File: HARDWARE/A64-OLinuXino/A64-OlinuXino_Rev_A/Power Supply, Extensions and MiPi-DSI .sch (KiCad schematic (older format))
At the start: 140 parts, among them Q2 MC-306_32.768KHZ/SMD_8038/6pF, Q3 4SB24.000F20E15/5x3.2mm/20ppm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, T1 WPM1481, U1 AllWinner-A64(FBGA396), U13 MT3608(SOT23-6), U14 AXP803

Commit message: A64-OLinuXino component placement, all components libraries updated
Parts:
- removed L15: FB0805/600R/2A, symbol L
- D1: renamed from D3; footprint (none) -> OLIMEX_Diodes-FP:DO214AA
- D4: footprint (none) -> OLIMEX_Diodes-FP:SOD-123_1C-2A_KA
- DBG_UART1: footprint (none) -> OLIMEX_Connectors-FP:HN1x3
- FET2: footprint (none) -> OLIMEX_Transistors-FP:SOT23
- FUSE2: footprint (none) -> OLIMEX_Devices-FP:FUSE-5025
- GPIO1: value GBH-254-SMT-40 -> NA(HN2x20); footprint (none) -> OLIMEX_Connectors-FP:HN2x20
- L14: renamed from L17; footprint (none) -> OLIMEX_RLC-FP:CD32
- L15: renamed from L18; footprint (none) -> OLIMEX_RLC-FP:CD42(43)
- L16: renamed from L14; footprint (none) -> OLIMEX_RLC-FP:YS75_7X8MM
- L17: renamed from L19; footprint (none) -> OLIMEX_RLC-FP:CD42(43)
- L18: renamed from L16; footprint (none) -> OLIMEX_RLC-FP:CD42(43)
- L19: renamed from L20; footprint (none) -> OLIMEX_RLC-FP:CD32
- L20: renamed from L21; footprint (none) -> OLIMEX_RLC-FP:CD32
- LIPO_BAT1: footprint (none) -> OLIMEX_Connectors-FP:LIPO_BAT-CON2DW02R
- MIPI-DSI1: value GPH127SMT-02X10(PA-V16X-2X10-LF) -> PV-WZA21-20-LF; footprint (none) -> OLIMEX_Connectors-FP:FPV-WZA21-20-LF
- PWR1: footprint (none) -> OLIMEX_Connectors-FP:PWR_JACK_UNI_MILLING
- PWRLED1: footprint (none) -> OLIMEX_LEDs-FP:LED_0603_KA
- PWRON1, RESET1, UBOOT1: footprint (none) -> OLIMEX_Buttons-FP:WS_TAKT_6X3,5_SMD_NOCREAM
- Q2: footprint (none) -> OLIMEX_Crystal-FP:MC306-HS
- Q3: footprint (none) -> OLIMEX_Crystal-FP:Q5x3.25
- RM14: footprint (none) -> OLIMEX_RLC-FP:RA0805_(4X0402)_xx
- T1: value WPM1481 -> WPM1481(DFN2X2-6L); footprint (none) -> OLIMEX_Transistors-FP:DFN2x2-6L
- U1: footprint (none) -> OLIMEX_IC-FP:FBGA396
- U13: footprint (none) -> OLIMEX_IC-FP:SOT23-6
- U14: value AXP803 -> AXP803(QFN68_8x8mm); footprint (none) -> OLIMEX_IC-FP:QFN68
- UEXT1: footprint (none) -> OLIMEX_Connectors-FP:GBH-254-SMT-10
- VCC-PE:2.8V/3.3V1: footprint (none) -> OLIMEX_Jumpers-FP:SJ_2_SMALL_12_TIED
- renumbered C171 to C115, C172 to C116, C173 to C117, C117 to C118, C118 to C119, C174 to C120, C133 to C121, C137 to C122, C175 to C123, C134 to C124, C138 to C125, C139 to C126, C176 to C127, C135 to C128, C140 to C129, C177 to C130, C141 to C131, C178 to C132, C142 to C133, C179 to C134, C136 to C135, C143 to C136, C180 to C137, C123 to C138, C144 to C139, C119 to C140, C120 to C141, C181 to C142, C115 to C143, C124 to C144, C182 to C146, C125 to C147, C183 to C148, C130 to C149, C146 to C150, C131 to C151, C132 to C152, C147 to C153, C148 to C154, C184 to C155, C121 to C156, C149 to C157, C185 to C158, C150 to C159, C186 to C160, C151 to C161, C152 to C162, C187 to C163, C153 to C164, C154 to C165, C188 to C166, C155 to C167, C189 to C168, C126 to C169, C156 to C170, C127 to C171, C157 to C172, C128 to C173, C158 to C174, C129 to C175, C159 to C176, C122 to C177, C160 to C178, C161 to C179, C116 to C180, C162 to C181, C163 to C182, C166 to C183, C167 to C184, C168 to C185, C190 to C186, C169 to C187, C191 to C188, C192 to C189, C193 to C190, C194 to C191, C195 to C192, C170 to C193, C164 to C194, C165 to C195, D1 to D2, D2 to D3, R76 to R74, R90 to R75, R91 to R76, R92 to R77, R87 to R78, R93 to R79, R74 to R80, R75 to R81, R80 to R82, R81 to R83, R88 to R84, R82 to R85, R83 to R86, R84 to R87, R85 to R88, R77 to R89, R86 to R90, R78 to R91, R89 to R92, R94 to R93, R95 to R94, R79 to R95
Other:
- note added: "GFC STILL NOT READ!"
- note added: "Notes:\n1.PC4 and PC7 could be used only when \nNAND Flash is not populated!\n2.VCC-PL is 1.8V, VCC-PE is 2.8V(default),\nVCC-PB and VCC-PC are 3.3V."
- note added: "The schematic was checked\nfrom Root up to Here!!!!!"
- note removed: "Note:\nPC4 and PC7 could be used only when \nNAND Flash is not populated!"

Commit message: A64-OLinuXino update
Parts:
- added C197: 100nF, OLIMEX_RLC-FP:C_0402_5MIL_DWS, symbol C
- added HSIC1: B4B-PH-K-S, OLIMEX_Connectors-FP:B4B-PH-K-S, symbol CON4
- added HSIC_E1: Opened, OLIMEX_Jumpers-FP:SJ, symbol SJ
- added R101, R102: NA(2.2k), OLIMEX_RLC-FP:R_0402_5MIL_DWS, symbol R
- added R103: NA(100k), OLIMEX_RLC-FP:R_0402_5MIL_DWS, symbol R
- added R104: NA(10k), OLIMEX_RLC-FP:R_0402_5MIL_DWS, symbol R
- PWRON1, RESET1, UBOOT1: footprint OLIMEX_Buttons-FP:WS_TAKT_6X3,5_SMD_NOCREAM -> OLIMEX_Buttons-FP:uTACTIL
- R74, R82: value 1k -> 2.2k; footprint OLIMEX_RLC-FP:R_0603_5MIL_DWS -> OLIMEX_RLC-FP:R_0402_5MIL_DWS
- R75, R76, R77, R79, R80, R81, R83, R84, R85, R86, R87, R88, R89, R90, R91, R92, R95: footprint OLIMEX_RLC-FP:R_0603_5MIL_DWS -> OLIMEX_RLC-FP:R_0402_5MIL_DWS
- R78: footprint OLIMEX_RLC-FP:R_0603_5MIL_DWS -> OLIMEX_RLC-FP:R_1206_5MIL_DWS
- UEXT1: footprint OLIMEX_Connectors-FP:GBH-254-SMT-10 -> OLIMEX_Connectors-FP:HN2x5
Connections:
- net +1.5V: now also U14.8 (DCDC5)
- net +3.0VA: now also R103.1
- net 1.1V_SYS: now also U14.9 (DCDC6)
- net 1.2V_HSIC: now also C197.1, HSIC_E1.1
- net 3.0V_RTC: now also R104.1
- net AP-RESET#: now also R104.2
- net GND: now also C197.2, HSIC1.4
- net KEYADC: now also R103.2
- net PE14: now also R101.1
- net PE15: now also R102.1
- net at L20.1, U14.10 (LX6): no longer U14.9 (DCDC6)
- net at L19.1, U14.7 (LX5): no longer U14.8 (DCDC5)
- net at C194.2, U1.U18 (VCC-PE), VCC-PE:2.8V/3.3V1.2: now also R101.2, R102.2
- net at U1.G19 (HSIC-DAT): now also HSIC1.3
- net at U1.H19 (HSIC-STR): now also HSIC1.2
- new net: HSIC1.1, HSIC_E1.2
- no-connect marks 4 -> 2
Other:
- note added: "+5VDC ONLY!!!"
- note added: "DC5SET DDR3-VCC\nFloating 1.24V\nGND 1.50V\nVINT 1.36V"
- note added: "DDR3-VCC"
- note added: "Notes:\n1.PC4 and PC7 could be used only when \nNAND Flash is not populated!\n2. VCC-PE is 2.8V(default),\nVCC-PB, VCC-PC and VCC-PL are 3.3V."
- note added: "VCC-PL=3.3V"
- note removed: "Notes:\n1.PC4 and PC7 could be used only when \nNAND Flash is not populated!\n2.VCC-PL is 1.8V, VCC-PE is 2.8V(default),\nVCC-PB and VCC-PC are 3.3V."
- note removed: "VCC-PL=1.8V"

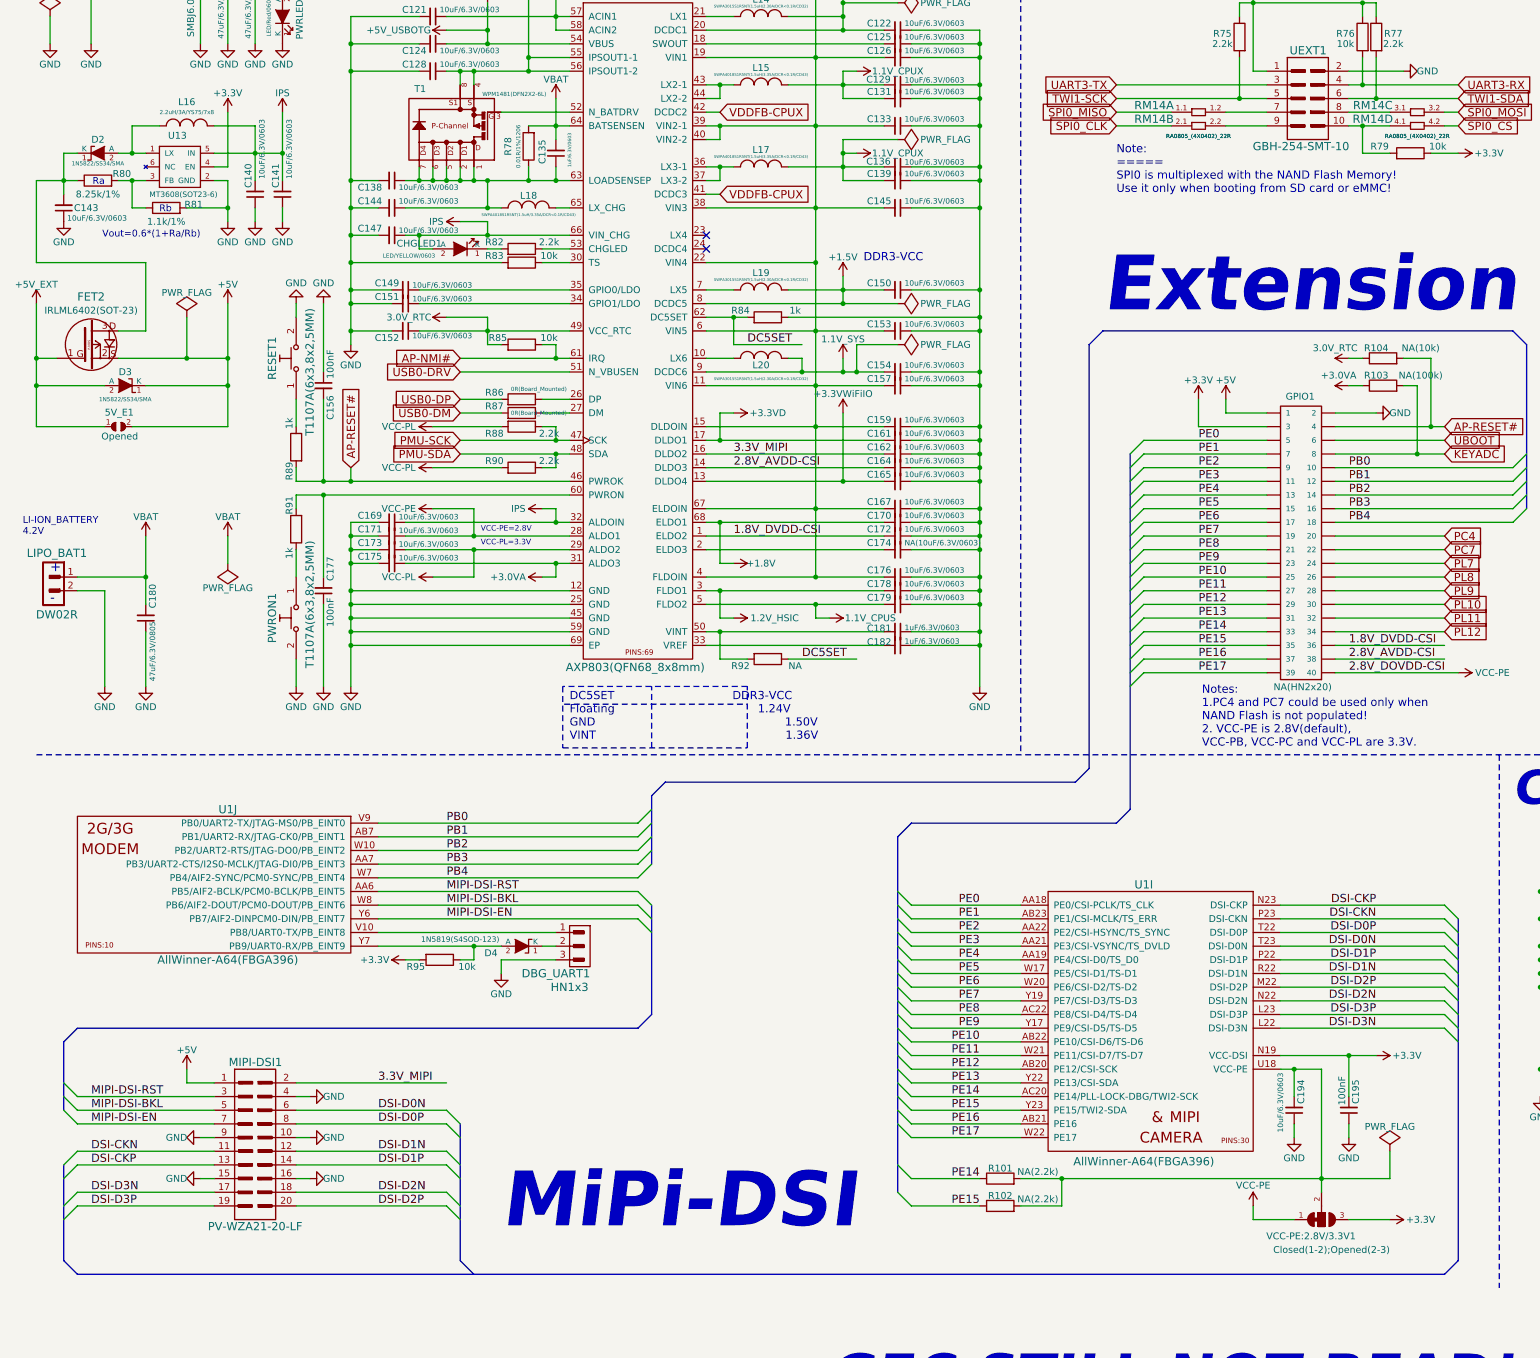
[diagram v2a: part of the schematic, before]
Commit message: A64-OLinuXino routing completed
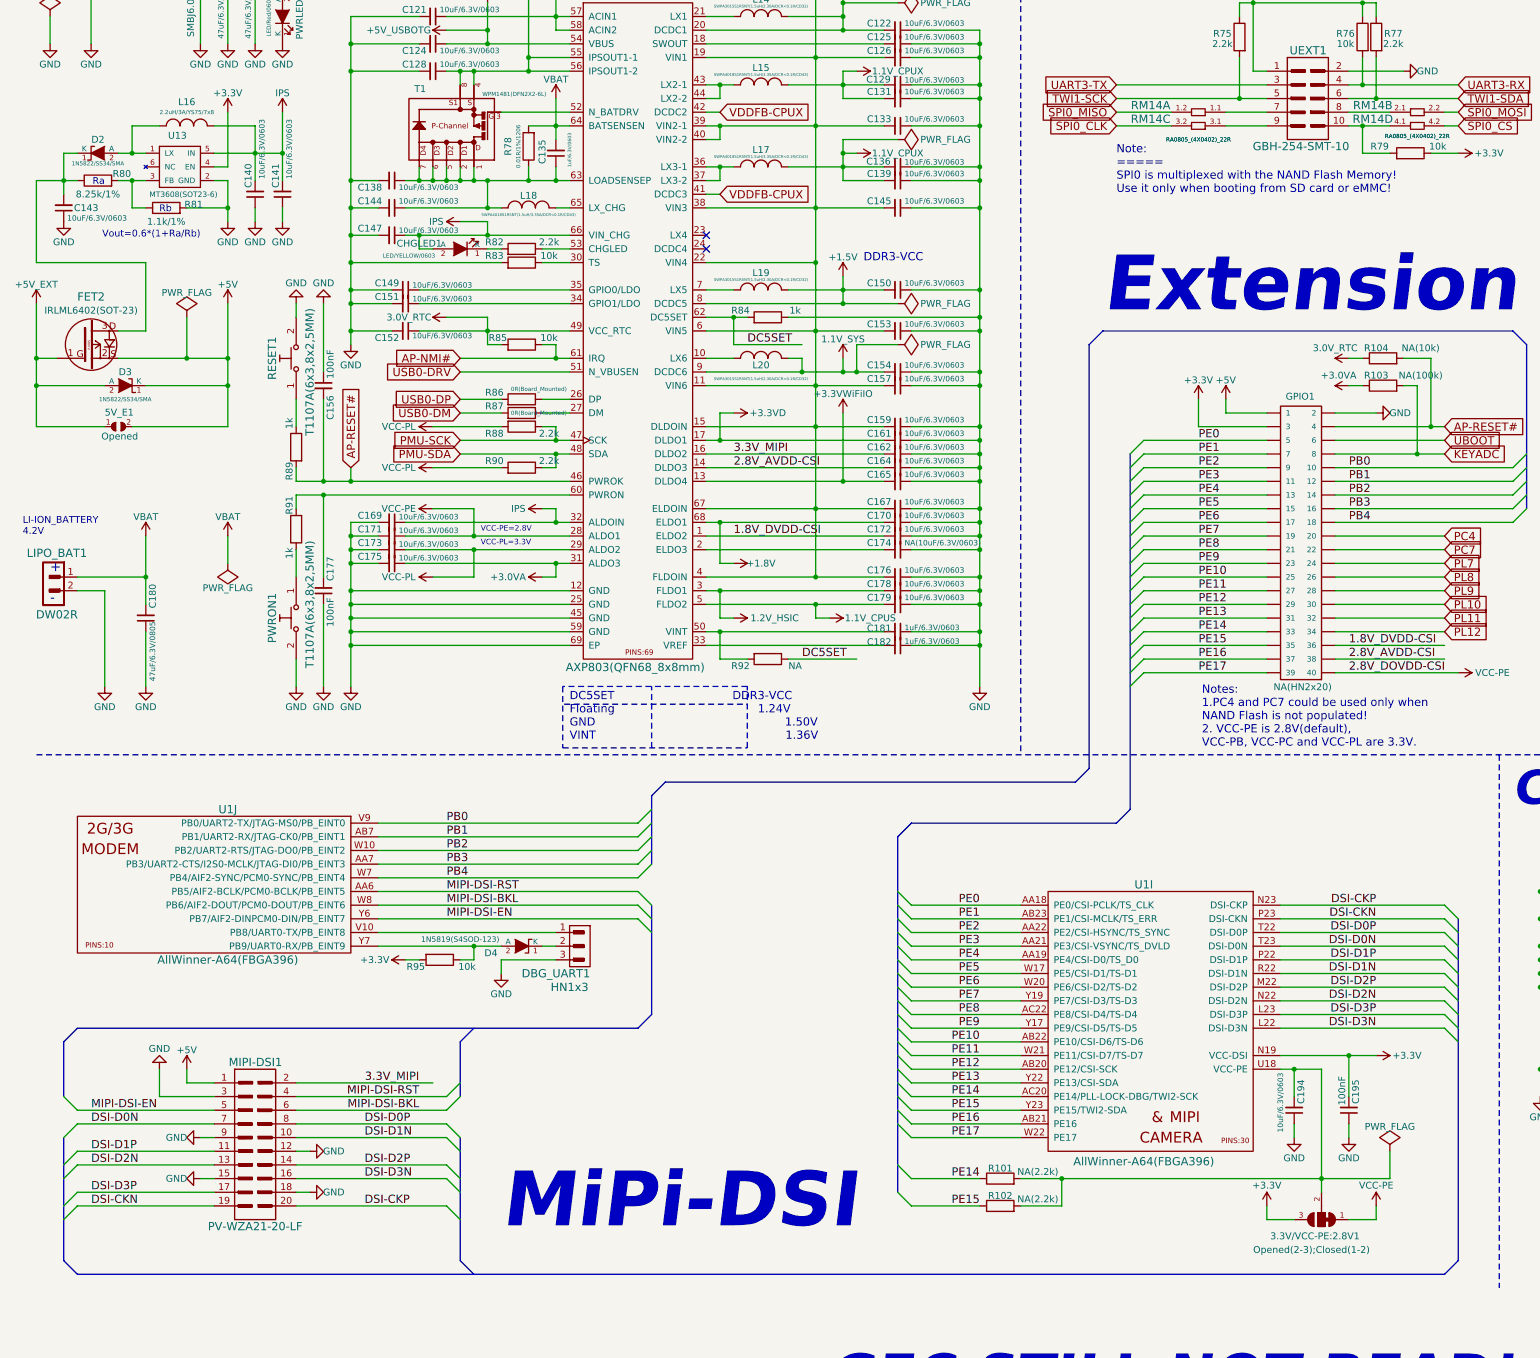
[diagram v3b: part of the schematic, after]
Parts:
- 3.3V/VCC-PE:2.8V1: renamed from VCC-PE:2.8V/3.3V1; value Closed(1-2);Opened(2-3) -> Opened(2-3);Closed(1-2)
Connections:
- net DSI-CKN: now also MIPI-DSI1.19; no longer MIPI-DSI1.11
- net DSI-CKP: now also MIPI-DSI1.20; no longer MIPI-DSI1.13
- net DSI-D0N: now also MIPI-DSI1.7; no longer MIPI-DSI1.6
- net DSI-D1N: now also MIPI-DSI1.10; no longer MIPI-DSI1.12
- net DSI-D1P: now also MIPI-DSI1.11; no longer MIPI-DSI1.14
- net DSI-D2N: now also MIPI-DSI1.13; no longer MIPI-DSI1.18
- net DSI-D2P: now also MIPI-DSI1.14; no longer MIPI-DSI1.20
- net DSI-D3N: now also MIPI-DSI1.16; no longer MIPI-DSI1.17
- net DSI-D3P: now also MIPI-DSI1.17; no longer MIPI-DSI1.19
- net GND: now also MIPI-DSI1.12, MIPI-DSI1.18, MIPI-DSI1.3; no longer MIPI-DSI1.10, MIPI-DSI1.16, MIPI-DSI1.4
- net MIPI-DSI-BKL: now also MIPI-DSI1.6; no longer MIPI-DSI1.5
- net MIPI-DSI-EN: now also MIPI-DSI1.5; no longer MIPI-DSI1.7
- net MIPI-DSI-RST: now also MIPI-DSI1.4; no longer MIPI-DSI1.3
- net SPI0_CLK: now also RM14.3.2; no longer RM14.2.1
- net SPI0_MISO: now also RM14.1.2; no longer RM14.1.1
- net SPI0_MOSI: now also RM14.2.2; no longer RM14.3.2
- net at UEXT1.7: now also RM14.1.1; no longer RM14.1.2
- net at RM14.3.1: now also UEXT1.9; no longer UEXT1.8
- new net: RM14.2.1, UEXT1.8
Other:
- moved on the sheet: RM14B, RM14C
